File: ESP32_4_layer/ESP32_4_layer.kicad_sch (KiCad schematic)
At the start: 0 parts

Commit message: delete
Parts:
- added J1: SS-52400-003, SS-52400-003:BELFUSE_SS-52400-003, symbol Mein_Library:SS-52400-003
- added J2: JST_S2B-PH-K-S_LF__SN_, S2B-PH-K-S_LF__SN_:JST_S2B-PH-K-S_LF__SN_, symbol Mein_Library:JST_S2B-PH-K-S_LF__SN_
- added U1: MCP73871-4CC, Package_DFN_QFN:QFN-20-1EP_4x4mm_P0.5mm_EP2.5x2.5mm, symbol Battery_Management:MCP73871-4CC
- added U2: LM1117MP-3.3, Package_TO_SOT_SMD:SOT-223-3_TabPin2, symbol Regulator_Linear:LM1117MP-3.3
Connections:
- new net: U1.1 (OUT), U1.20 (OUT)
- new net: U1.10 (V_{SS}), U1.11 (V_{SS}), U1.21 (V_{SS})
- new net: U1.14 (V_{BAT}), U1.15 (V_{BAT})
- new net: U1.18 (IN), U1.19 (IN)
- new net GND/SHIELD: J1.G1 (GND/SHIELD), J1.G2 (GND/SHIELD), J1.G3 (GND/SHIELD), J1.G4 (GND/SHIELD), J1.S1 (GND/SHIELD), J1.S2 (GND/SHIELD), J1.S3 (GND/SHIELD), J1.S4 (GND/SHIELD)

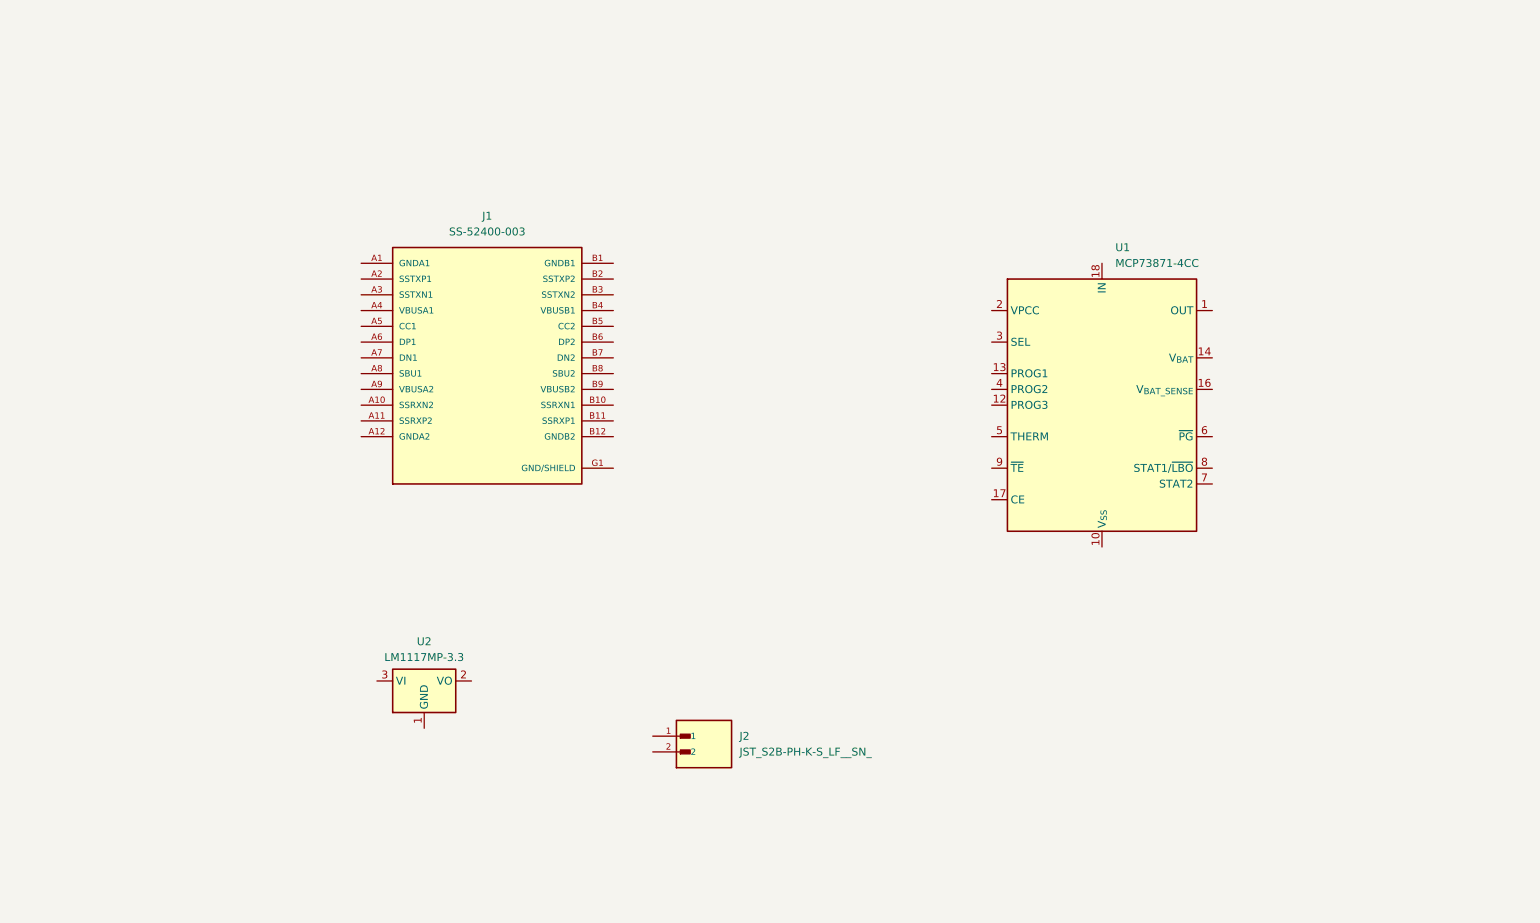
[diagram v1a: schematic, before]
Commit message: USB-C connector and Lipo battery charger schematic completed
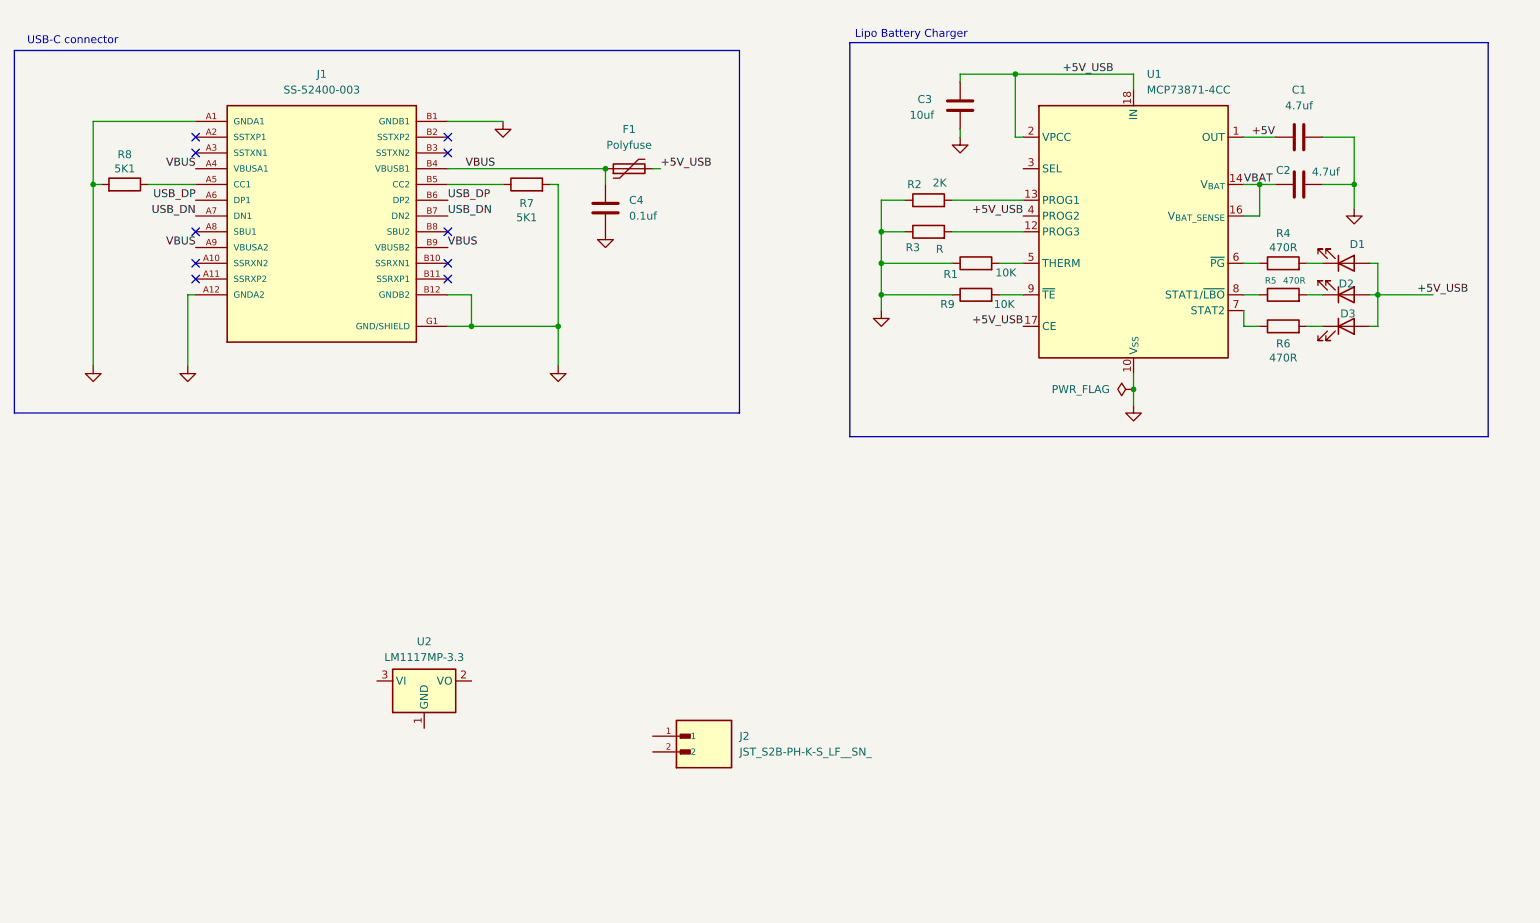
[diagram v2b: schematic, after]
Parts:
- added C1, C2: 4.7uf, symbol Device:C
- added C3: 10uf, symbol Device:C
- added C4: 0.1uf, symbol Device:C
- added D1, D2, D3: LED, symbol Device:LED
- added F1: Polyfuse, symbol Device:Polyfuse
- added R1, R9: 10K, symbol Device:R
- added R2: 2K, symbol Device:R
- added R3: R, symbol Device:R
- added R4, R5, R6: 470R, symbol Device:R
- added R7, R8: 5K1, symbol Device:R
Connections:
- net GND/SHIELD is gone; now on net GND: J1.G1 (GND/SHIELD), J1.G2 (GND/SHIELD), J1.G3 (GND/SHIELD), J1.G4 (GND/SHIELD), J1.S1 (GND/SHIELD), J1.S2 (GND/SHIELD), J1.S3 (GND/SHIELD), J1.S4 (GND/SHIELD)
- net GND: now reaches J1.A1 (GNDA1)
- net GND: now also J1.A12 (GNDA2), J1.B1 (GNDB1), J1.B12 (GNDB2), U1.10 (V_{SS}), U1.11 (V_{SS}), U1.21 (V_{SS}), C1.2, C2.2, C3.1, C4.1, R1.1, R2.1, R3.1, R7.2, R8.2, R9.1
- net VBUS: now reaches J1.A4 (VBUSA1)
- net VBUS: now also J1.A9 (VBUSA2), J1.B4 (VBUSB1), J1.B9 (VBUSB2), C4.2, F1.1
- net at J1.A5 (CC1): now also R8.1
- net USB_DP: now reaches J1.A6 (DP1)
- net USB_DP: now also J1.B6 (DP2)
- net USB_DN: now reaches J1.A7 (DN1)
- net USB_DN: now also J1.B7 (DN2)
- net at J1.B5 (CC2): now also R7.1
- net +5V: now reaches U1.1 (OUT), U1.20 (OUT)
- net +5V: now also C1.1
- net at U1.12 (PROG3): now also R3.2
- net at U1.13 (PROG1): now also R2.2
- net VBAT: now reaches U1.14 (V_{BAT}), U1.15 (V_{BAT})
- net VBAT: now also U1.16 (V_{BAT_SENSE}), C2.1
- net +5V_USB: now reaches U1.17 (CE)
- net +5V_USB: now also U1.18 (IN), U1.19 (IN), U1.2 (VPCC), U1.4 (PROG2), C3.2, D1.2 (A), D2.2 (A), D3.2 (A), F1.2
- net at U1.5 (THERM): now also R1.2
- net at U1.6 (~{PG}): now also R4.1
- net at U1.7 (STAT2): now also R6.1
- net at U1.8 (STAT1/~{LBO}): now also R5.1
- net at U1.9 (~{TE}): now also R9.2
- new net: D2.1 (K), R6.2
- new net: D3.1 (K), R5.2
- new net: D1.1 (K), R4.2
- no-connect marks 0 -> 10
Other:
- note added: "Lipo Battery Charger"
- note added: "USB-C connector"
- moved on the sheet: J1, U1

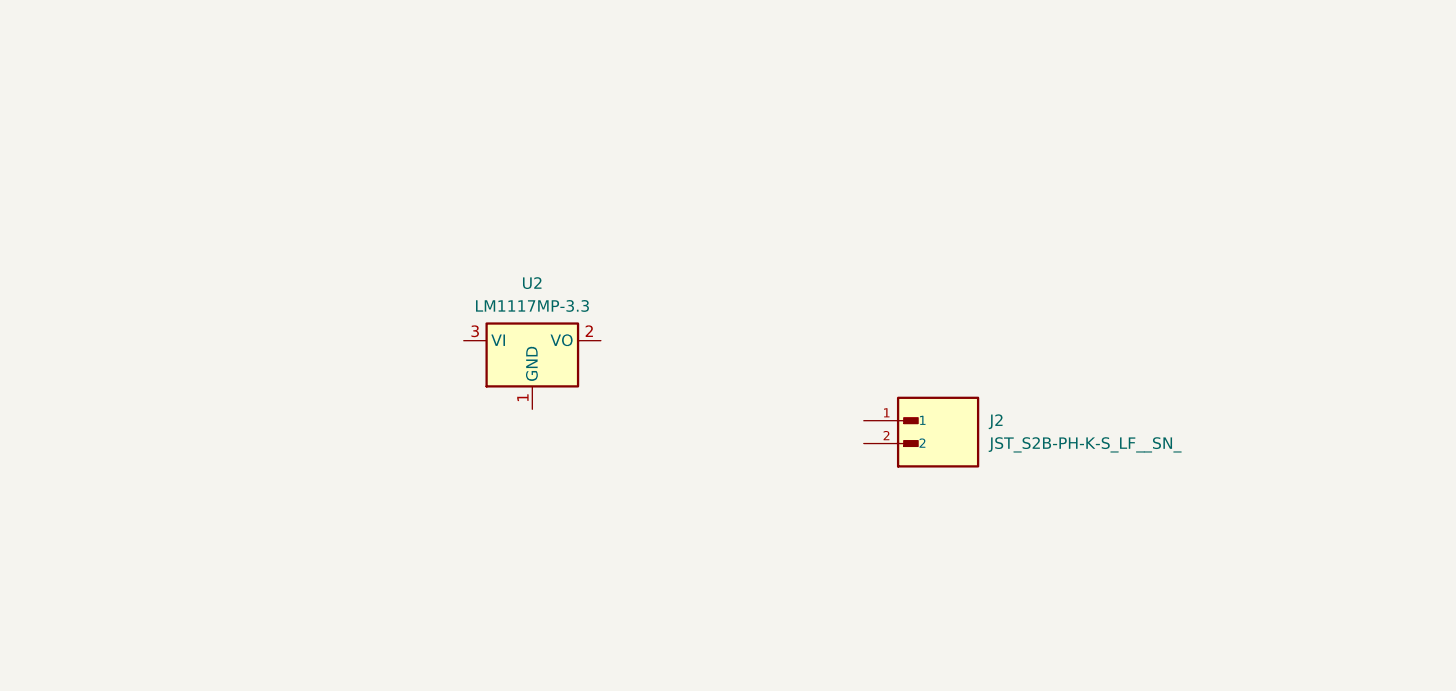
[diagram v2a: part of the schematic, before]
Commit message: LDO schematic completed
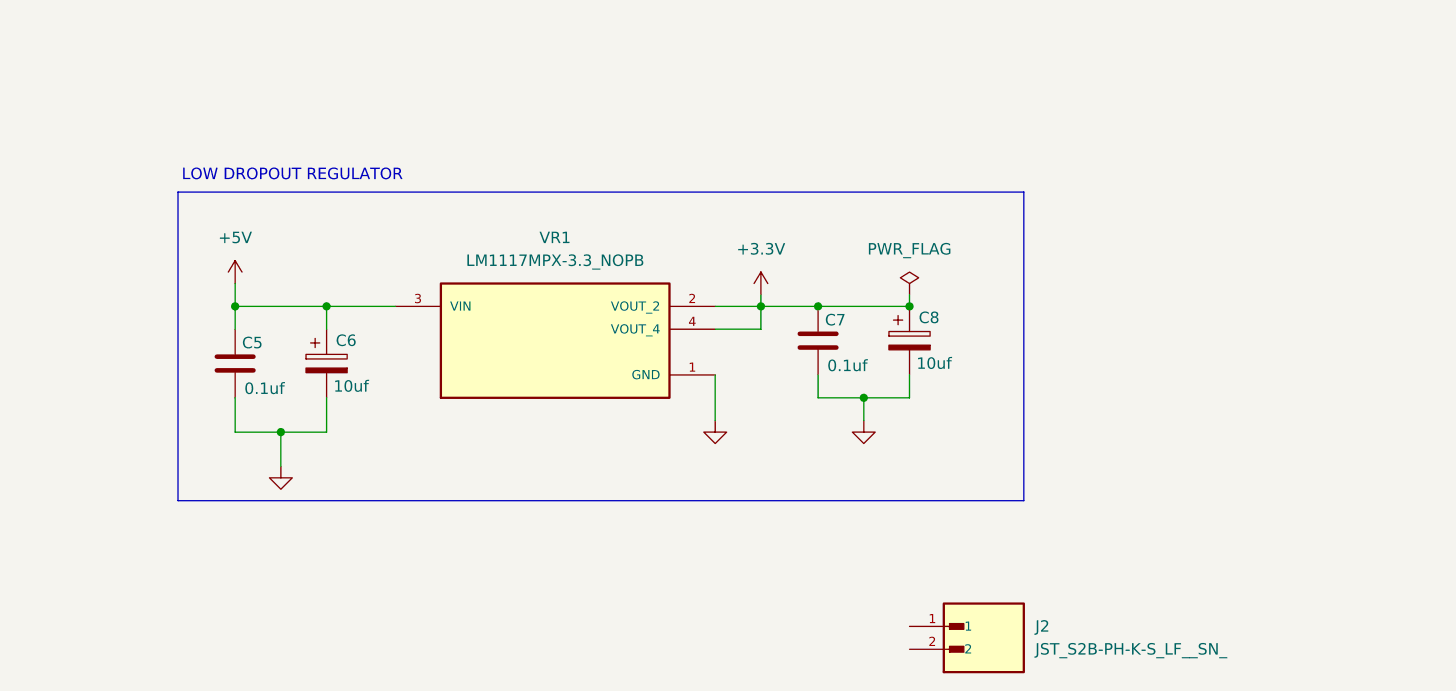
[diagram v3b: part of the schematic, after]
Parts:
- removed U2: LM1117MP-3.3, Package_TO_SOT_SMD:SOT-223-3_TabPin2, symbol Regulator_Linear:LM1117MP-3.3
- added C5, C7: 0.1uf, symbol Device:C
- added C6, C8: 10uf, symbol Device:C_Polarized
- added VR1: LM1117MPX-3.3_NOPB, LM1117MPX-3.3_NOPB:VREG_LM1117MPX-3.3_NOPB, symbol Own_Library:LM1117MPX-3.3_NOPB
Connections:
- net +5V: now also C5.1, C6.1, VR1.3 (VIN)
- net GND: now also C5.2, C6.2, C7.2, C8.2, VR1.1 (GND)
- new net +3.3V: C7.1, C8.1, VR1.2 (VOUT_2), VR1.4 (VOUT_4)
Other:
- note added: "LOW DROPOUT REGULATOR"
- moved on the sheet: J2

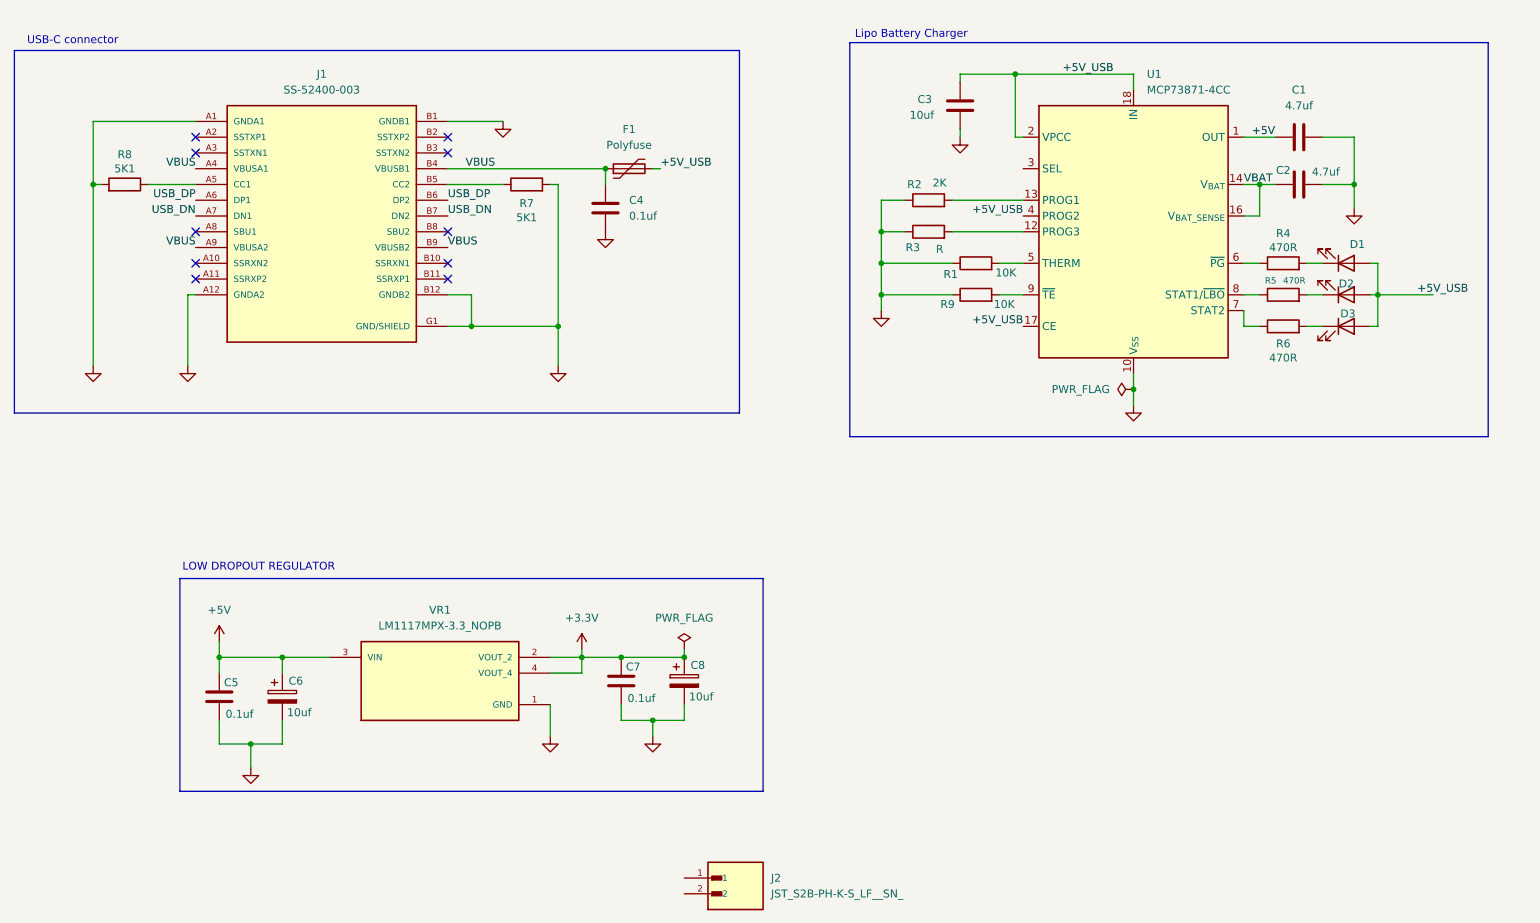
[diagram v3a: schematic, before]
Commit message: Battery connector and power indicator schematic competed
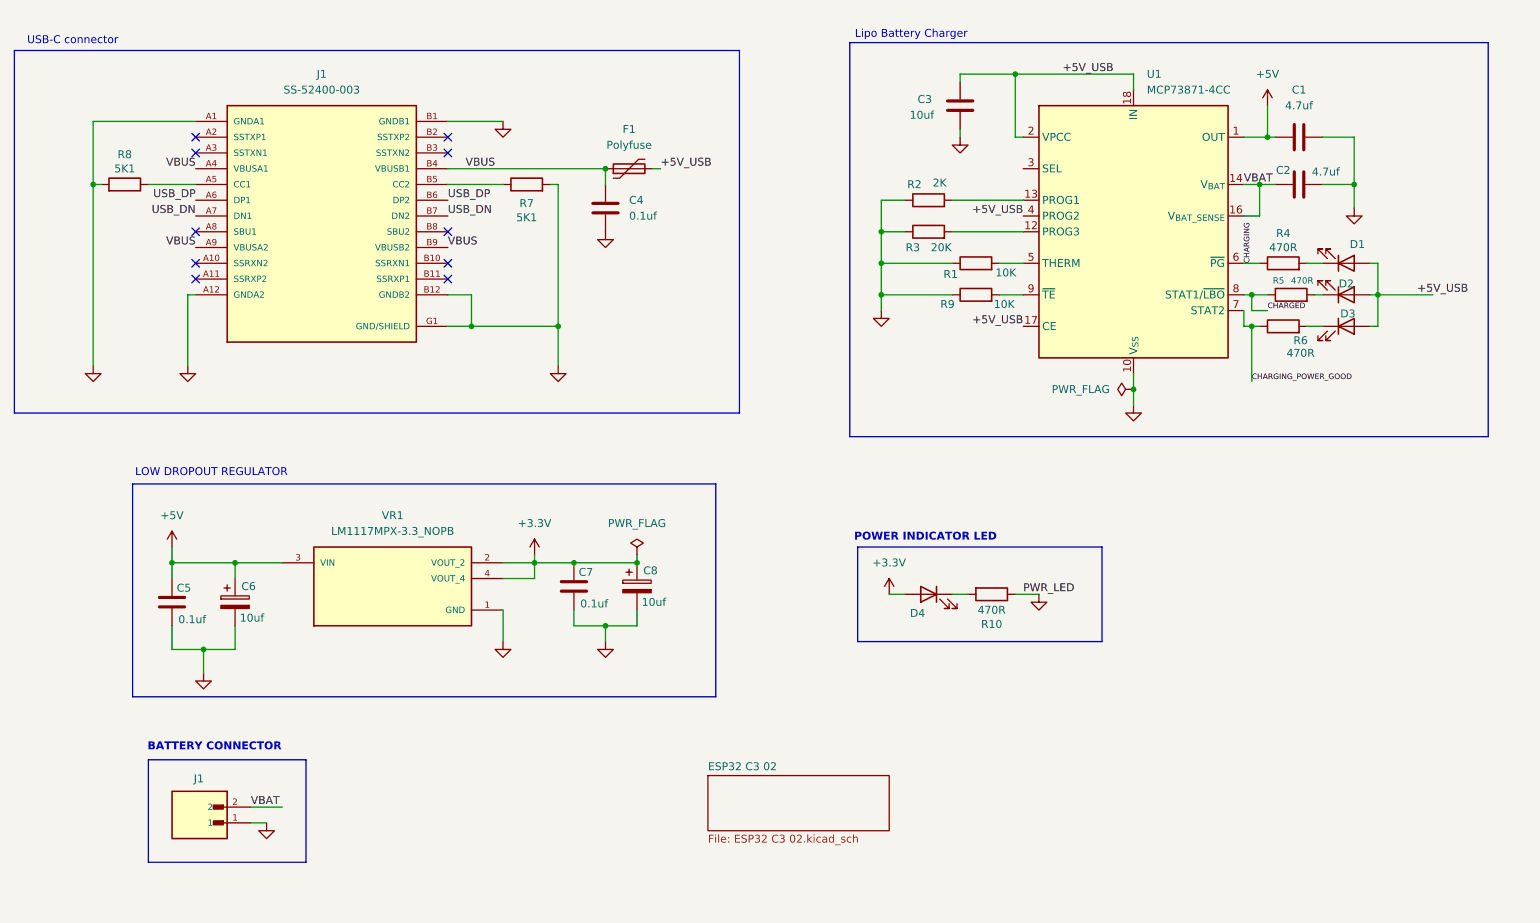
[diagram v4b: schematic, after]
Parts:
- added D4: LED, symbol Device:LED
- added R10: 470R, symbol Device:R
- R3: value R -> 20K
- renumbered J2 to J1
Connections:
- net +3.3V: now also D4.2 (A)
- net GND: now also J1.1, R10.1
- net VBAT: now also J1.2
- net CHARGING: now reaches R4.1, U1.6 (~{PG})
- net CHARGING_POWER_GOOD: now reaches R6.1, U1.7 (STAT2)
- net CHARGED: now reaches R5.1, U1.8 (STAT1/~{LBO})
- new net: D4.1 (K), R10.2
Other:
- added sheet ESP32 C3 02 (ESP32 C3 02.kicad_sch)
- note added: "BATTERY CONNECTOR"
- note added: "POWER INDICATOR LED"
- moved on the sheet: C5, C6, C7, C8, J1, R5, VR1

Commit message: second sheet added and components placed
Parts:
- renumbered J1 to J2
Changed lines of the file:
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@@
 		(on_board yes)
 		(dnp no)
-		(property "Reference" "J1"
+		(property "Reference" "J2"
 			(at 48.768 141.478 0)
 			(effects
@@
 			(project ""
 				(path "/052df048-a7d0-4515-b7e6-6d4a36313ca3"
-					(reference "J1")
+					(reference "J2")
 					(unit 1)
 				)
@@
 	)
 	(sheet
-		(at 130.81 140.97)
-		(size 29.21 8.89)
+		(at 229.87 138.43)
+		(size 27.94 6.35)
 		(exclude_from_sim no)
 		(in_bom yes)
@@
 			(width 0.1524)
 			(type solid)
+			(color 255 0 46 1)
 		)
 		(fill
-			(color 0 0 0 0.0000)
+			(color 255 0 23 1.0000)
 		)
 		(property "Sheetname" "ESP32 C3 02"
-			(at 130.81 140.2584 0)
+			(at 229.87 137.7184 0)
 			(effects
 				(font
@@
 		)
 		(property "Sheetfile" "ESP32 C3 02.kicad_sch"
-			(at 130.81 150.4446 0)
-			(effects
-				(font
+			(at 229.87 145.3646 0)
+			(effects
+				(font

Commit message: SENSORS COMPLETED
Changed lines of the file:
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@@
 	(wire
 		(pts
+			(xy 175.26 135.89) (xy 171.45 135.89)
+		)
+		(stroke
+			(width 0)
+			(type default)
+		)
+	)
+	(wire
+		(pts
 			(xy 219.71 45.72) (xy 219.71 50.8)
 		)
@@
 	(wire
 		(pts
+			(xy 175.26 138.43) (xy 171.45 138.43)
+		)
+		(stroke
+			(width 0)
+			(type default)
+		)
+	)
+	(wire
+		(pts
 			(xy 102.87 109.22) (xy 102.87 106.68)
 		)
@@
 	(wire
 		(pts
+			(xy 175.26 142.24) (xy 171.45 142.24)
+		)
+		(stroke
+			(width 0)
+			(type default)
+		)
+	)
+	(wire
+		(pts
 			(xy 49.53 120.65) (xy 49.53 124.46)
 		)
@@
 		)
 	)
+	(label "USB_DP"
+		(at 175.26 138.43 0)
+		(effects
+			(font
+				(size 1.27 1.27)
+			)
+			(justify left bottom)
+		)
+	)
 	(label "VBUS"
 		(at 48.26 43.18 180)
@@
 		)
 	)
+	(label "VBUS"
+		(at 175.26 142.24 0)
+		(effects
+			(font
+				(size 1.27 1.27)
+			)
+			(justify left bottom)
+		)
+	)
 	(label "CHARGED"
 		(at 220.98 66.04 0)
@@
 		)
 	)
+	(label "USB_DN"
+		(at 175.26 135.89 0)
+		(effects
+			(font
+				(size 1.27 1.27)
+			)
+			(justify left bottom)
+		)
+	)
 	(label "+5V_USB"
 		(at 245.11 63.5 0)
@@
 		)
 	)
+	(hierarchical_label "USB_DP"
+		(shape input)
+		(at 171.45 138.43 180)
+		(effects
+			(font
+				(size 1.27 1.27)
+			)
+			(justify right)
+		)
+	)
+	(hierarchical_label "USB_DN"
+		(shape input)
+		(at 171.45 135.89 180)
+		(effects
+			(font
+				(size 1.27 1.27)
+			)
+			(justify right)
+		)
+	)
+	(hierarchical_label "VBUS"
+		(shape input)
+		(at 171.45 142.24 180)
+		(effects
+			(font
+				(size 1.27 1.27)
+			)
+			(justify right)
+		)
+	)
 	(symbol
 		(lib_id "Own_Library:LM1117MPX-3.3_NOPB")
@@
 	)
 	(sheet
-		(at 229.87 138.43)
-		(size 27.94 6.35)
+		(at 143.51 133.35)
+		(size 27.94 16.51)
 		(exclude_from_sim no)
 		(in_bom yes)
@@
 		)
 		(property "Sheetname" "ESP32 C3 02"
-			(at 229.87 137.7184 0)
+			(at 143.51 132.6384 0)
 			(effects
 				(font
@@
 		)
 		(property "Sheetfile" "ESP32 C3 02.kicad_sch"
-			(at 229.87 145.3646 0)
+			(at 143.51 150.4446 0)
 			(effects
 				(font
